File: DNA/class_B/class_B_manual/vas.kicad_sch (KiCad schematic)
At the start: 7 parts, among them Q1 2N5551, Q2 FZT953, Q3 2N5551

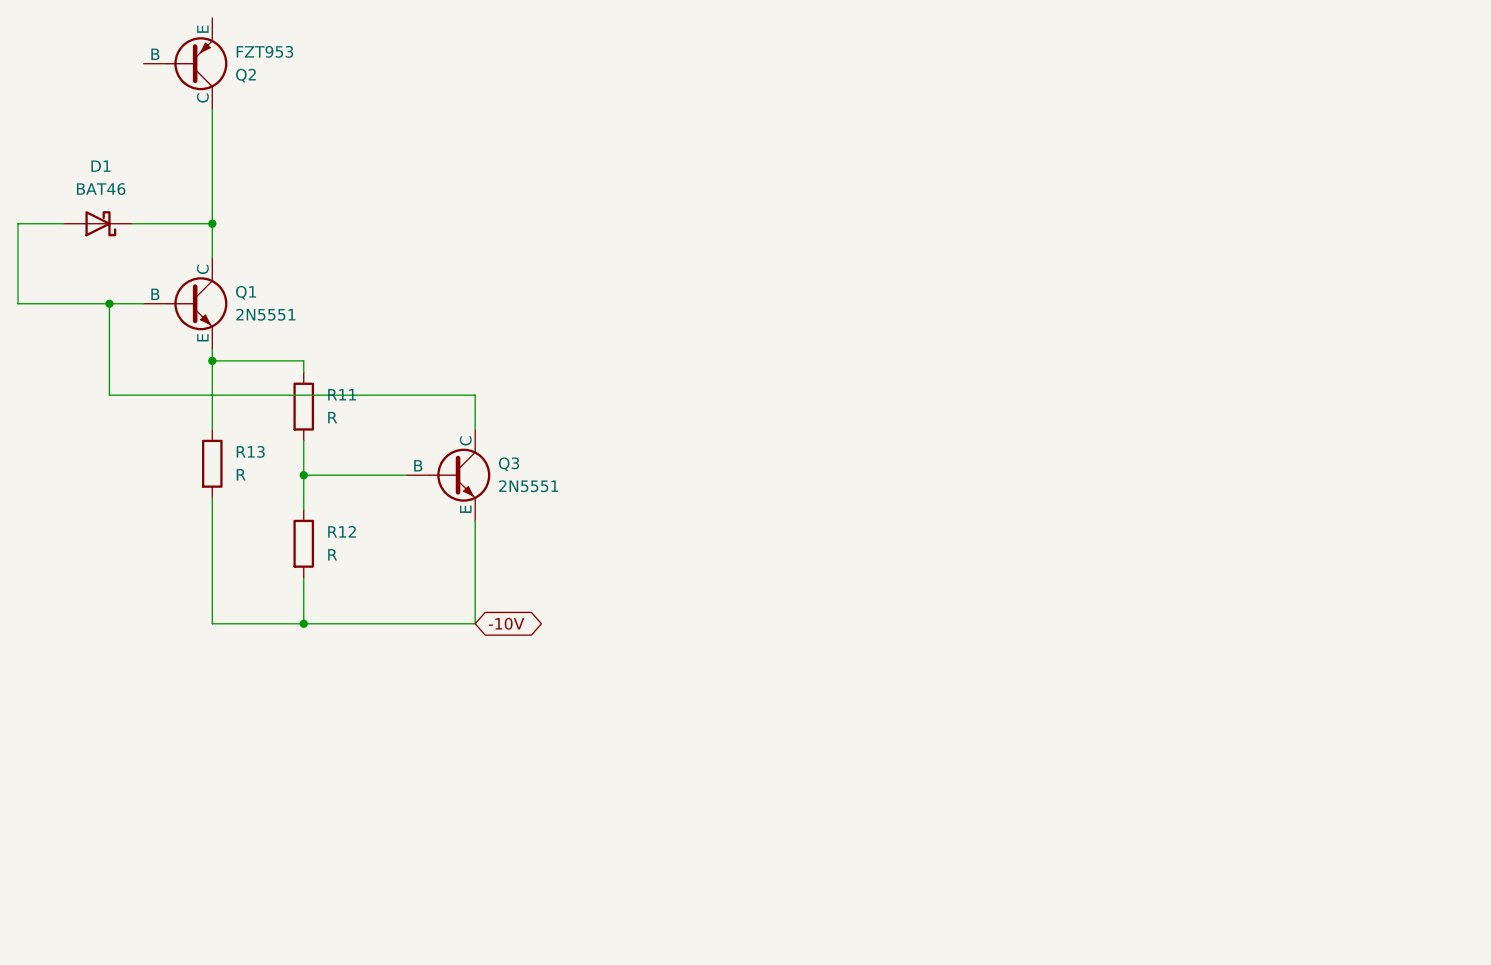
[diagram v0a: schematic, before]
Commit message: [DNA]: all the schematics for Class B amplifier is ready.
TODO: 1. Add resistors', capacitors' values. 2. Add all footprints for resistors and connectors.
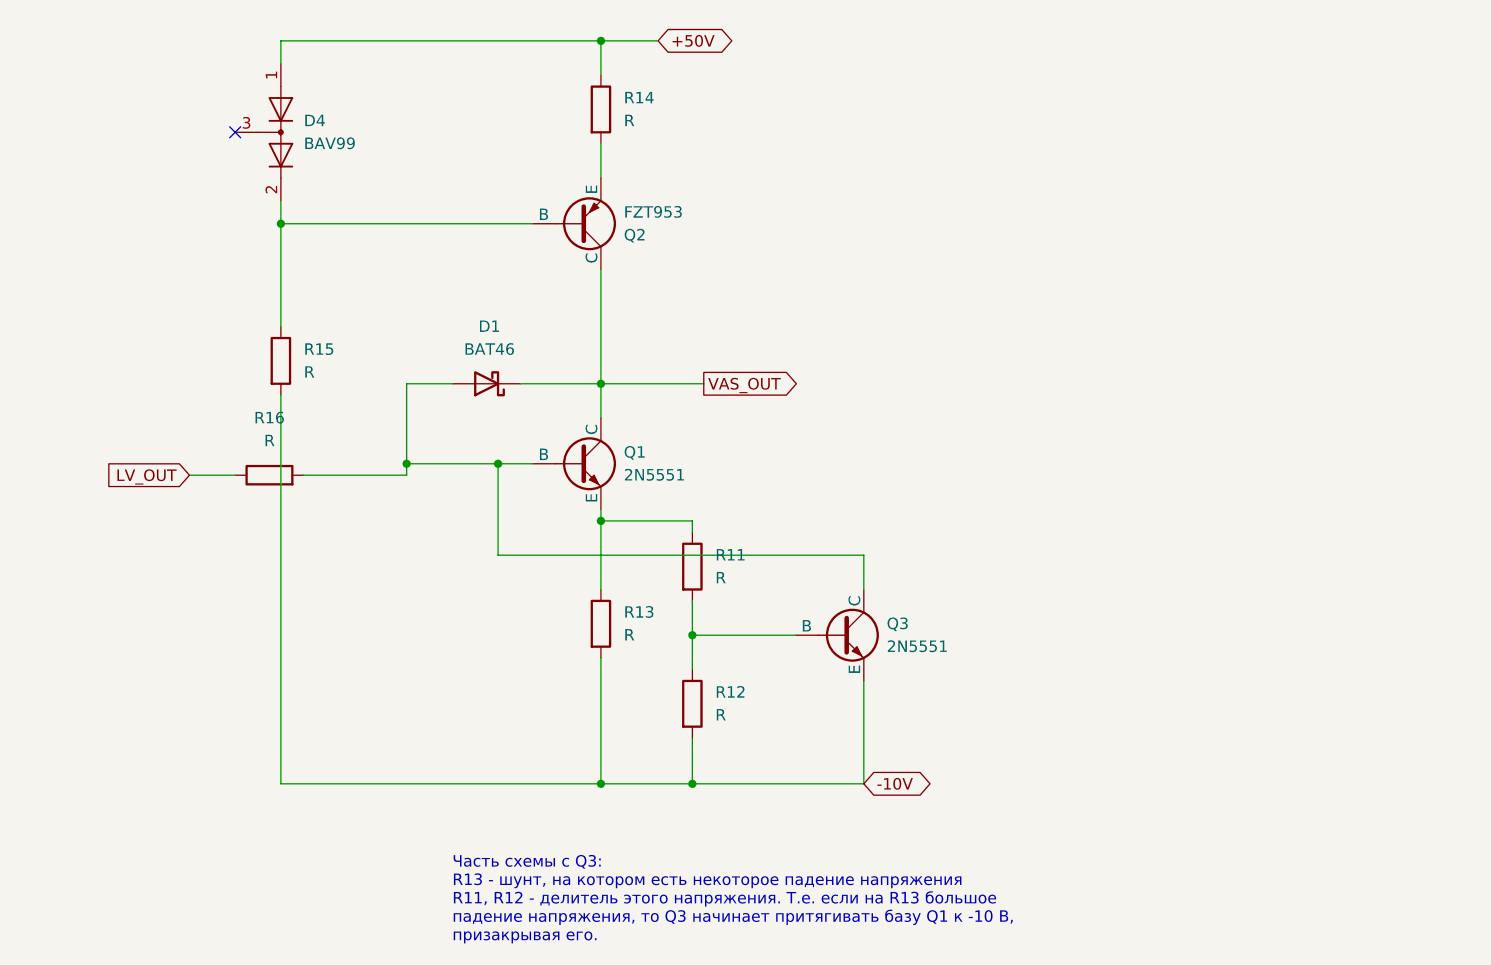
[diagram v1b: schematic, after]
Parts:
- added D4: BAV99, Package_TO_SOT_SMD:SOT-23, symbol Diode:BAV99
- added R14, R15, R16: R, symbol Device:R
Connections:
- net -10V: now also R15.2
- net at D1.2 (A), Q1.2 (B), Q3.3 (C): now also R16.2
- net VAS_OUT: now reaches D1.1 (K), Q1.3 (C), Q2.2 (C)
- net at Q2.1 (B): now also D4.2 (A), R15.1
- net at Q2.3 (E): now also R14.2
- new net +50V: D4.1 (K), R14.1
- new net LV_OUT: R16.1
- no-connect marks 0 -> 1
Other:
- note added: "Часть схемы с Q3: R13 - шунт, на котором есть некоторое падение напряжения R11, R12 - делитель этого напряжения. Т.е. если на R13 большое падение напряжения, то Q3 начинает притягивать базу Q1 к -10 В, призакрывая его."
- moved on the sheet: D1, Q1, Q2, Q3, R11, R12, R13

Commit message: [DNA]: class B: hierarchical labels added.
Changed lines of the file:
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@@
+    (stroke (width 0) (type default))
+  )
+  (wire (pts (xy 142.24 76.2) (xy 142.24 80.01))
     (stroke (width 0) (type default))
   )
@@
     (stroke (width 0) (type default))
   )
+  (wire (pts (xy 85.09 86.36) (xy 85.09 90.17))
+    (stroke (width 0) (type default))
+  )
   (text "Часть схемы с Q3:\nR13 - шунт, на котором есть некоторое падение напряжения\nR11, R12 - делитель этого напряжения. Т.е. если на R13 большое\nпадение напряжения, то Q3 начинает притягивать базу Q1 к -10 В,\nпризакрывая его."
     (at 114.3 142.24 0)
@@
     )
   )
+  (hierarchical_label "VAS_OUT" (shape output) (at 142.24 76.2 0) (fields_autoplaced)
+    (effects (font (size 1.27 1.27)) (justify left))
+  )
+  (hierarchical_label "LV_OUT" (shape input) (at 85.09 86.36 180) (fields_autoplaced)
+    (effects (font (size 1.27 1.27)) (justify right))
+  )
   (symbol (lib_id "Diode:BAV99") (at 95.25 52.07 270) (unit 1)

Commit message: [DNA]: class B, resistor values etc added.
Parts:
- R11: value R -> 4.7k
- R12: value R -> 1k
- R13: value R -> 150
- R14: value R -> 82
- R15: value R -> 11k
- R16: value R -> 47
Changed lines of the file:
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@@
       (effects (font (size 1.27 1.27)) (justify left))
     )
-    (property "Value" "R" (at 133.35 50.8 0)
+    (property "Value" "82" (at 133.35 50.8 0)
       (effects (font (size 1.27 1.27)) (justify left))
     )
@@
       (effects (font (size 1.27 1.27)) (justify left))
     )
-    (property "Value" "R" (at 143.51 116.84 0)
+    (property "Value" "1k" (at 143.51 116.84 0)
       (effects (font (size 1.27 1.27)) (justify left))
     )
@@
       (effects (font (size 1.27 1.27)) (justify left))
     )
-    (property "Value" "R" (at 143.51 101.6 0)
+    (property "Value" "4.7k" (at 143.51 101.6 0)
       (effects (font (size 1.27 1.27)) (justify left))
     )
@@
       (effects (font (size 1.27 1.27)) (justify left))
     )
-    (property "Value" "R" (at 133.35 107.95 0)
+    (property "Value" "150" (at 133.35 107.95 0)
       (effects (font (size 1.27 1.27)) (justify left))
     )
@@
       (effects (font (size 1.27 1.27)))
     )
-    (property "Value" "R" (at 93.98 86.36 90)
+    (property "Value" "47" (at 93.98 86.36 90)
       (effects (font (size 1.27 1.27)))
     )
@@
       (effects (font (size 1.27 1.27)) (justify left))
     )
-    (property "Value" "R" (at 97.79 78.74 0)
+    (property "Value" "11k" (at 97.79 78.74 0)
       (effects (font (size 1.27 1.27)) (justify left))
     )
